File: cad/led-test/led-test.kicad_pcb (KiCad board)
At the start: 2 copper layers, 26.7 x 15.2 mm, 3 parts

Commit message: more kicad learning
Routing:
- net Net-(BT1-Pad1): track 8.89 -> 0.00 mm
- net Net-(BT1-Pad2): track 8.89 -> 8.15 mm
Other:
- board size 26.7 x 15.2 mm -> 27.9 x 21.6 mm
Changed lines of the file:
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@@
   (general
     (thickness 1.6)
-    (drawings 4)
+    (drawings 9)
     (tracks 4)
     (zones 0)
@@
       (drillshape 0)
       (scaleselection 1)
-      (outputdirectory "./"))
+      (outputdirectory "./gerber/"))
   )
   (net 0 "")
@@
     )
   )
-  (gr_line (start 118.11 -1062.99) (end 118.11 -1078.23) (layer Edge.Cuts) (width 0.15))
-  (gr_line (start 144.78 -1062.99) (end 118.11 -1062.99) (layer Edge.Cuts) (width 0.15))
-  (gr_line (start 144.78 -1078.23) (end 144.78 -1062.99) (layer Edge.Cuts) (width 0.15))
-  (gr_line (start 118.11 -1078.23) (end 144.78 -1078.23) (layer Edge.Cuts) (width 0.15))
+  (gr_line (start 118.11 -1075.69) (end 129.54 -1084.58) (layer Edge.Cuts) (width 0.15))
+  (gr_line (start 116.84 -1065.53) (end 118.11 -1075.69) (layer Edge.Cuts) (width 0.15))
+  (gr_line (start 121.92 -1062.99) (end 116.84 -1065.53) (layer Edge.Cuts) (width 0.15))
+  (gr_line (start 142.24 -1064.26) (end 121.92 -1062.99) (layer Edge.Cuts) (width 0.15))
+  (gr_line (start 144.78 -1066.8) (end 142.24 -1064.26) (layer Edge.Cuts) (width 0.15))
+  (gr_line (start 144.78 -1073.15) (end 144.78 -1066.8) (layer Edge.Cuts) (width 0.15))
+  (gr_line (start 142.24 -1078.23) (end 144.78 -1073.15) (layer Edge.Cuts) (width 0.15))
+  (gr_line (start 138.43 -1082.04) (end 142.24 -1078.23) (layer Edge.Cuts) (width 0.15))
+  (gr_line (start 129.54 -1084.58) (end 138.43 -1082.04) (layer Edge.Cuts) (width 0.15))
   (segment (start 139.7 -1074.42) (end 139.7 -1069.34) (width 0.25) (layer F.Cu) (net 1))
-  (segment (start 130.81 -1069.34) (end 130.81 -1074.42) (width 0.25) (layer F.Cu) (net 2))
-  (segment (start 130.81 -1074.42) (end 134.62 -1074.42) (width 0.25) (layer F.Cu) (net 2))
-  (segment (start 139.7 -1066.8) (end 130.81 -1066.8) (width 0.25) (layer F.Cu) (net 3))
+  (segment (start 130.81 -1069.34) (end 133.35 -1069.34) (width 0.25) (layer F.Cu) (net 2))
+  (segment (start 133.35 -1069.34) (end 134.62 -1070.61) (width 0.25) (layer F.Cu) (net 2))
+  (segment (start 134.62 -1070.61) (end 134.62 -1074.42) (width 0.25) (layer F.Cu) (net 2))
+  (zone (net 0) (net_name "") (layer F.Cu) (hatch edge 0.508)
+    (connect_pads (clearance 0.508))
+    (min_thickness 0.254)
+    (keepout (tracks not_allowed) (vias not_allowed) (copperpour allowed))
+    (fill (arc_segments 16) (thermal_gap 0.508) (thermal_bridge_width 0.508))
+    (polygon
+      (pts
+        (xy 122.81554 -1077.363784) (xy 122.81554 -1076.093784) (xy 129.16554 -1073.553784) (xy 129.16554 -1078.633784) (xy 127.89554 -1078.633784)
+      )
+    )
+  )
 )

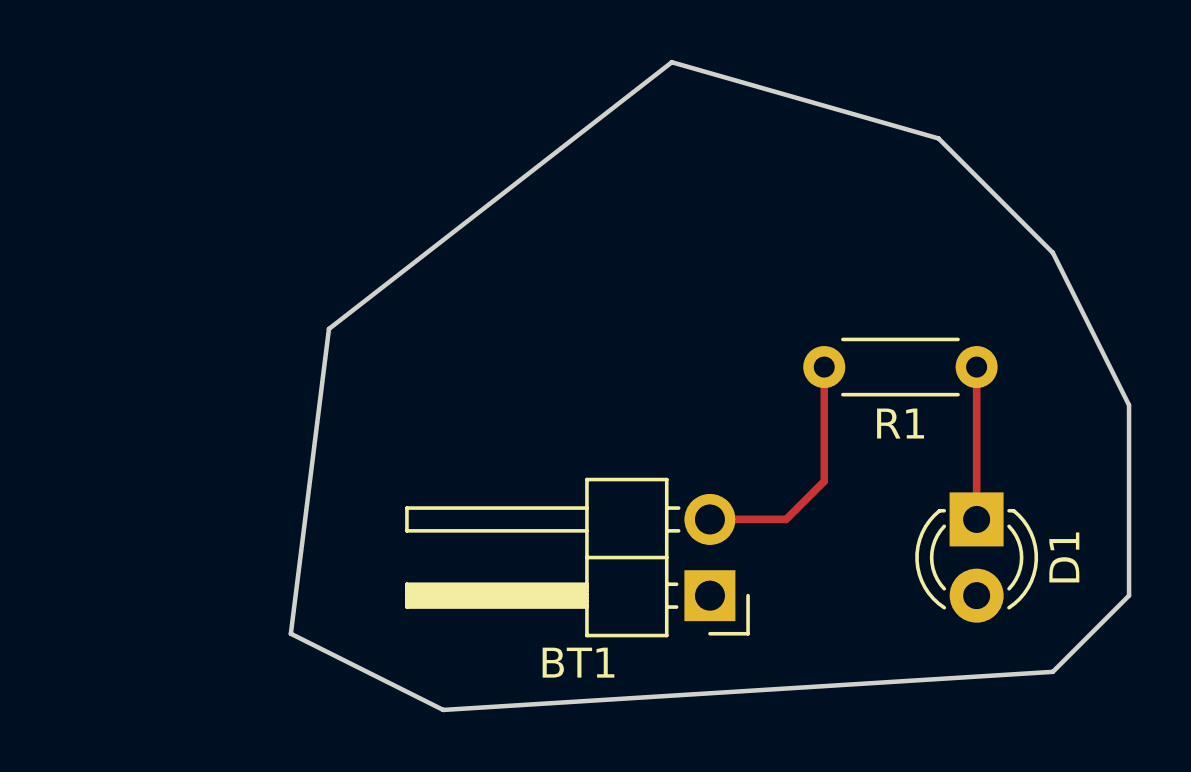
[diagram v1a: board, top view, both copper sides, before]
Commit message: added stop light tht and smd folders
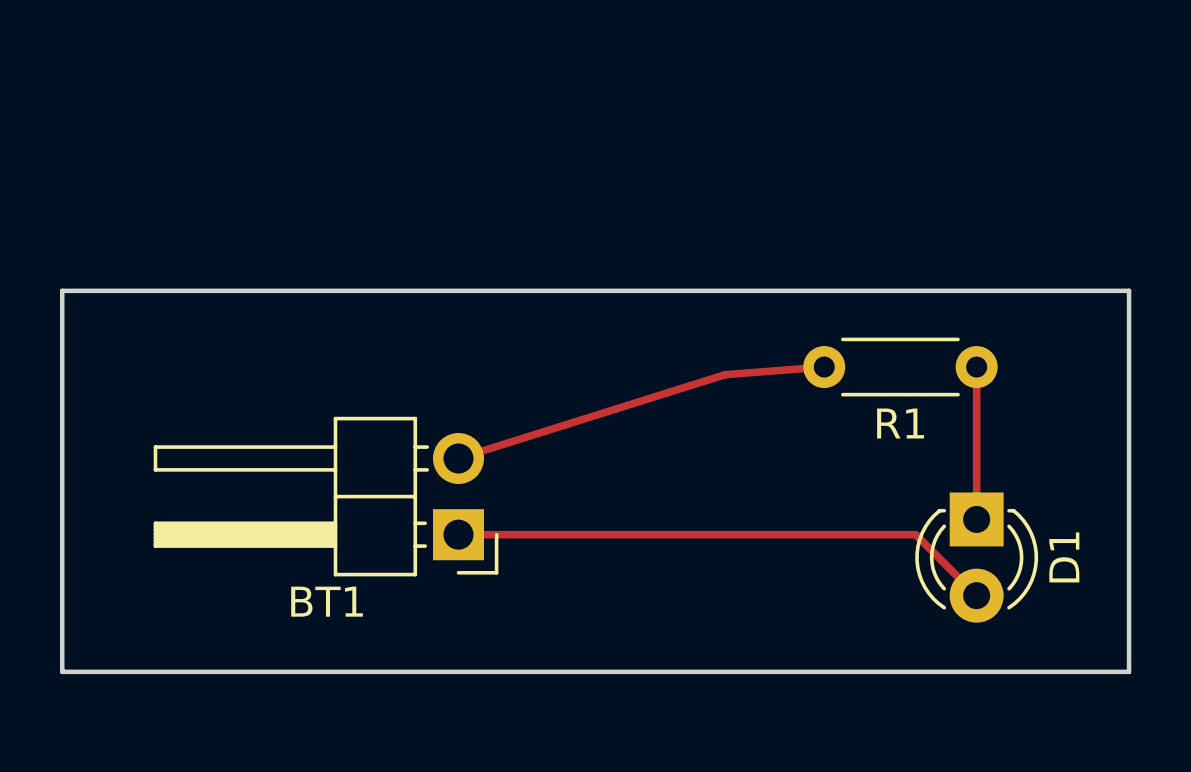
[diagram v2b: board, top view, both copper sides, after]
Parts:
- moved BT1 8.62 mm to (122.4, -1068.8)
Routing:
- net Net-(BT1-Pad1): track 0.00 -> 18.1 mm
- net Net-(BT1-Pad2): track 8.15 -> 12.6 mm
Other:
- board size 27.9 x 21.6 mm -> 35.6 x 12.7 mm
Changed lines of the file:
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@@
   (general
     (thickness 1.6)
-    (drawings 9)
-    (tracks 4)
+    (drawings 4)
+    (tracks 6)
     (zones 0)
     (modules 3)
@@
   (layers
     (0 F.Cu signal)
-    (31 B.Cu signal)
-    (32 B.Adhes user)
+    (31 B.Cu signal hide)
     (33 F.Adhes user)
-    (34 B.Paste user)
     (35 F.Paste user)
-    (36 B.SilkS user)
     (37 F.SilkS user)
     (38 B.Mask user)
@@
     (46 B.CrtYd user)
     (47 F.CrtYd user)
-    (48 B.Fab user)
     (49 F.Fab user)
   )
@@
     (add_net "Net-(D1-Pad1)")
   )
-  (module Connector_PinHeader_2.54mm:PinHeader_1x02_P2.54mm_Horizontal (layer F.Cu)
-    (at 130.81 -1066.8 180)
+  (module Connector_PinHeader_2.54mm:PinHeader_1x02_P2.54mm_Horizontal locked (layer F.Cu)
+    (at 122.428 -1068.832 180)
     (descr "Through hole angled pin header, 1x02, 2.54mm pitch, 6mm pin length, single row")
     (tags "Through hole angled pin header THT 1x02 2.54mm single row")
@@
       (effects (font (size 1 1) (thickness 0.15)))
     )
-    (fp_text value 330 (at 2.54 1.92 180) (layer F.Fab)
+    (fp_text value 330 (at -2.54 0 180) (layer F.Fab)
       (effects (font (size 1 1) (thickness 0.15)))
     )
@@
     )
   )
-  (gr_line (start 118.11 -1075.69) (end 129.54 -1084.58) (layer Edge.Cuts) (width 0.15))
-  (gr_line (start 116.84 -1065.53) (end 118.11 -1075.69) (layer Edge.Cuts) (width 0.15))
-  (gr_line (start 121.92 -1062.99) (end 116.84 -1065.53) (layer Edge.Cuts) (width 0.15))
-  (gr_line (start 142.24 -1064.26) (end 121.92 -1062.99) (layer Edge.Cuts) (width 0.15))
-  (gr_line (start 144.78 -1066.8) (end 142.24 -1064.26) (layer Edge.Cuts) (width 0.15))
-  (gr_line (start 144.78 -1073.15) (end 144.78 -1066.8) (layer Edge.Cuts) (width 0.15))
-  (gr_line (start 142.24 -1078.23) (end 144.78 -1073.15) (layer Edge.Cuts) (width 0.15))
-  (gr_line (start 138.43 -1082.04) (end 142.24 -1078.23) (layer Edge.Cuts) (width 0.15))
-  (gr_line (start 129.54 -1084.58) (end 138.43 -1082.04) (layer Edge.Cuts) (width 0.15))
-  (segment (start 139.7 -1074.42) (end 139.7 -1069.34) (width 0.25) (layer F.Cu) (net 1))
-  (segment (start 130.81 -1069.34) (end 133.35 -1069.34) (width 0.25) (layer F.Cu) (net 2))
-  (segment (start 133.35 -1069.34) (end 134.62 -1070.61) (width 0.25) (layer F.Cu) (net 2))
-  (segment (start 134.62 -1070.61) (end 134.62 -1074.42) (width 0.25) (layer F.Cu) (net 2))
-  (zone (net 0) (net_name "") (layer F.Cu) (hatch edge 0.508)
-    (connect_pads (clearance 0.508))
-    (min_thickness 0.254)
-    (keepout (tracks not_allowed) (vias not_allowed) (copperpour allowed))
-    (fill (arc_segments 16) (thermal_gap 0.508) (thermal_bridge_width 0.508))
-    (polygon
-      (pts
-        (xy 122.81554 -1077.363784) (xy 122.81554 -1076.093784) (xy 129.16554 -1073.553784) (xy 129.16554 -1078.633784) (xy 127.89554 -1078.633784)
-      )
-    )
-  )
+  (gr_line (start 109.22 -1076.96) (end 144.78 -1076.96) (layer Edge.Cuts) (width 0.15))
+  (gr_line (start 109.22 -1064.26) (end 109.22 -1076.96) (layer Edge.Cuts) (width 0.15))
+  (gr_line (start 144.78 -1064.26) (end 109.22 -1064.26) (layer Edge.Cuts) (width 0.15))
+  (gr_line (start 144.78 -1076.96) (end 144.78 -1064.26) (layer Edge.Cuts) (width 0.15))
+  (segment (start 139.7 -1070.49) (end 139.7 -1074.42) (width 0.25) (layer F.Cu) (net 1))
+  (segment (start 139.7 -1069.34) (end 139.7 -1070.49) (width 0.25) (layer F.Cu) (net 1))
+  (segment (start 131.318 -1074.166) (end 134.62 -1074.42) (width 0.25) (layer F.Cu) (net 2))
+  (segment (start 122.428 -1071.372) (end 131.318 -1074.166) (width 0.25) (layer F.Cu) (net 2))
+  (segment (start 137.668 -1068.832) (end 139.7 -1066.8) (width 0.25) (layer F.Cu) (net 3))
+  (segment (start 122.428 -1068.832) (end 137.668 -1068.832) (width 0.25) (layer F.Cu) (net 3))
 )
